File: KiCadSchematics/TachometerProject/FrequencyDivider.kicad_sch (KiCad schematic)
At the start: 7 parts, among them U1 74LS90, U2 74LS90

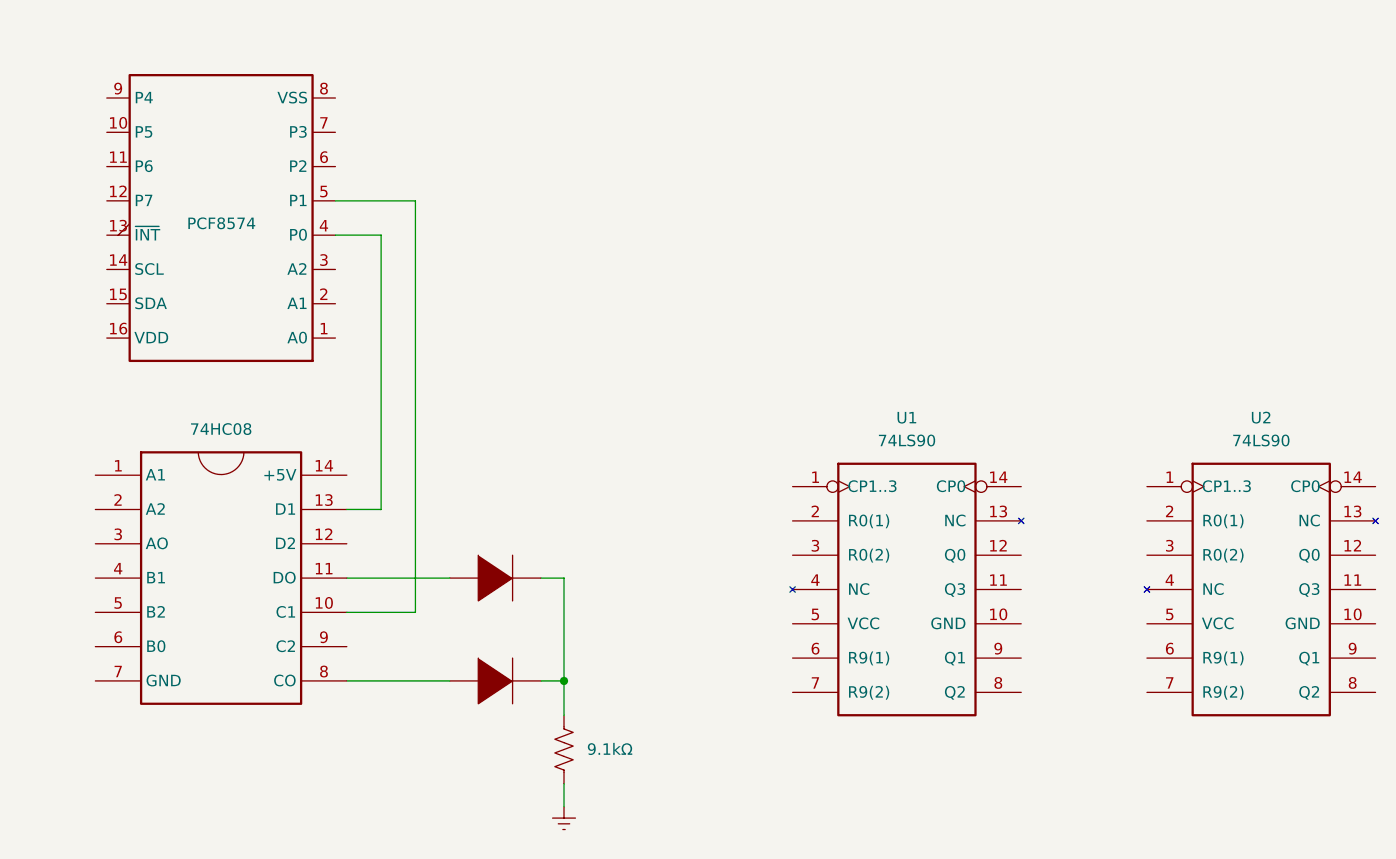
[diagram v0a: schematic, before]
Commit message: Added frequency divider
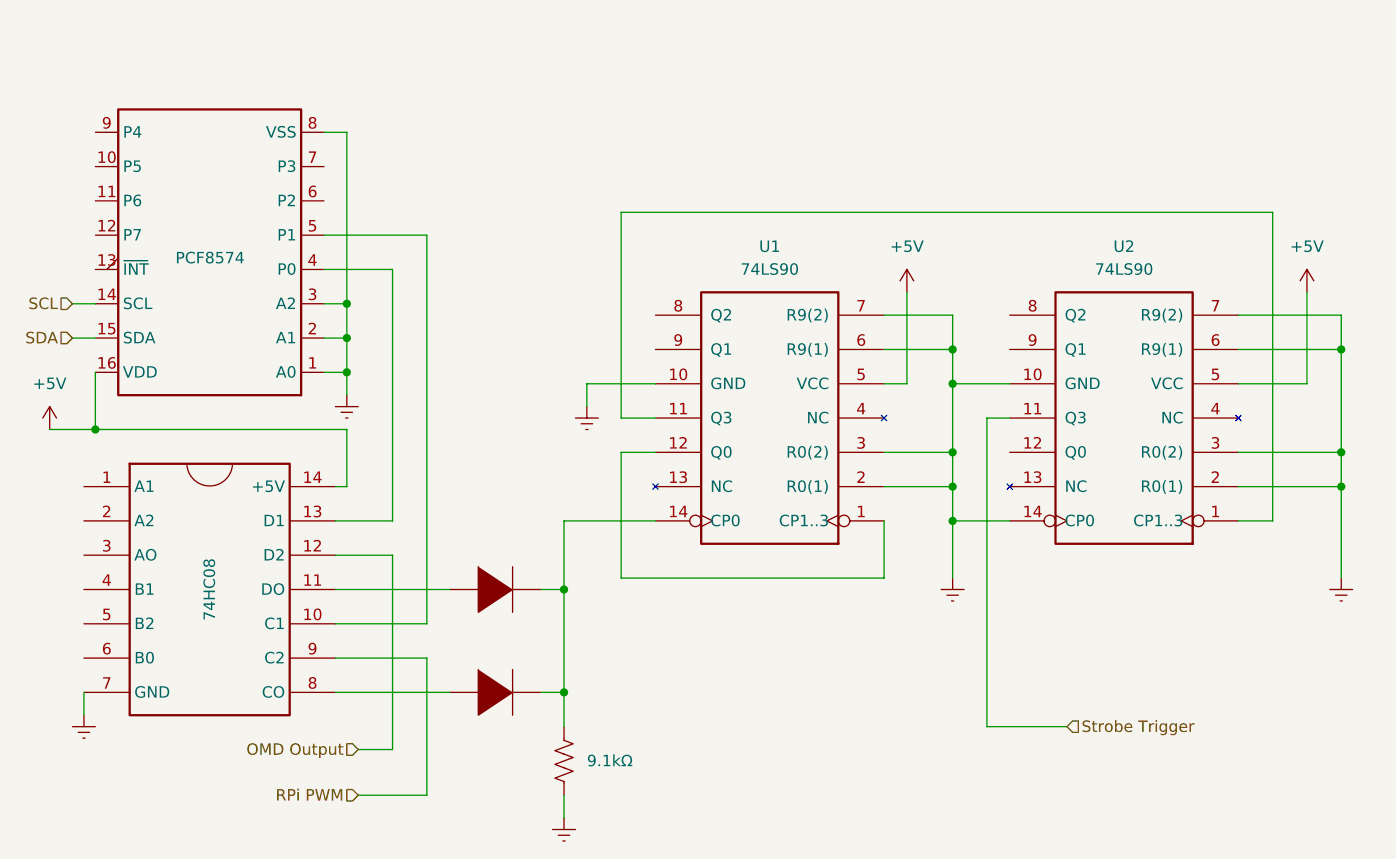
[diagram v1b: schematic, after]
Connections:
- net Earth: now also U1.10 (GND), U1.2 (R0(1)), U1.3 (R0(2)), U1.6 (R9(1)), U1.7 (R9(2)), U2.10 (GND), U2.14 (CP0), U2.2 (R0(1)), U2.3 (R0(2)), U2.6 (R9(1)), U2.7 (R9(2)), U?.1 (A0), U?.2 (A1), U?.3 (A2), U?.7 (GND), U?.8 (VSS)
- net at D?.2 (A), D?.2 (A), R?.1: now also U1.14 (CP0)
- net at U1.1 (CP1..3): now also U1.12 (Q0)
- net at U1.11 (Q3): now also U2.1 (CP1..3)
- net +5V: now reaches U1.5 (VCC)
- net +5V: now also U2.5 (VCC), U?.14 (+5V), U?.16 (VDD)
- net SCL: now reaches U?.14 (SCL)
- net SDA: now reaches U?.15 (SDA)
- net Strobe Trigger: now reaches U2.11 (Q3)
- net OMD Output: now reaches U?.12 (D2)
- net RPi PWM: now reaches U?.9 (C2)
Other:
- moved on the sheet: U1, U2

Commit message: Updated circuit diagrams
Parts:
- removed D? (x2): DIODE, symbol pspice:DIODE
- removed R?: 9.1kΩ, symbol Device:R_US
- removed U1, U2: 74LS90, symbol 74xx:74LS90
- removed U?: 74HC08, symbol EGR_270:74HC08
- added U?: DG419, symbol EGR_270:DG419
- added U?: 74HC390, symbol EGR_270:74HC390
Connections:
- net +5V: now also U?.16 (Vcc), U?.4 (V+), U?.5 (VL)
- net Earth: now also U?.14 (2CLR), U?.2 (1CLR), U?.3 (GND), U?.7 (V-), U?.8 (GND)
- net OMD Output: now also U?.2 (S1)
- net RPi PWM: now also U?.8 (S2)
- net Strobe Trigger: now also U?.9 (2QD)
- net at U?.4 (P0): now also U?.6 (IN)
- new net: U?.1 (D), U?.4 (1CKB)
- new net: U?.1 (1CKA), U?.7 (1QD)
- new net: U?.12 (2CKB), U?.3 (1QA)
